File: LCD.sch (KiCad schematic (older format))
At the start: 5 parts

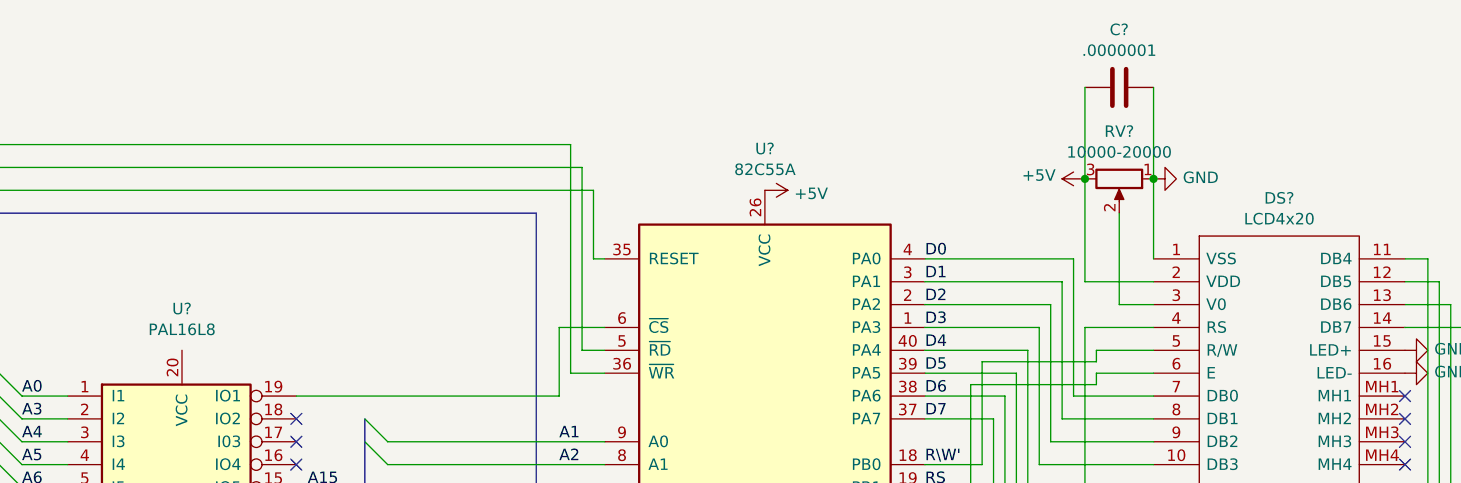
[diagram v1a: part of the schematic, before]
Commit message: All schematics present
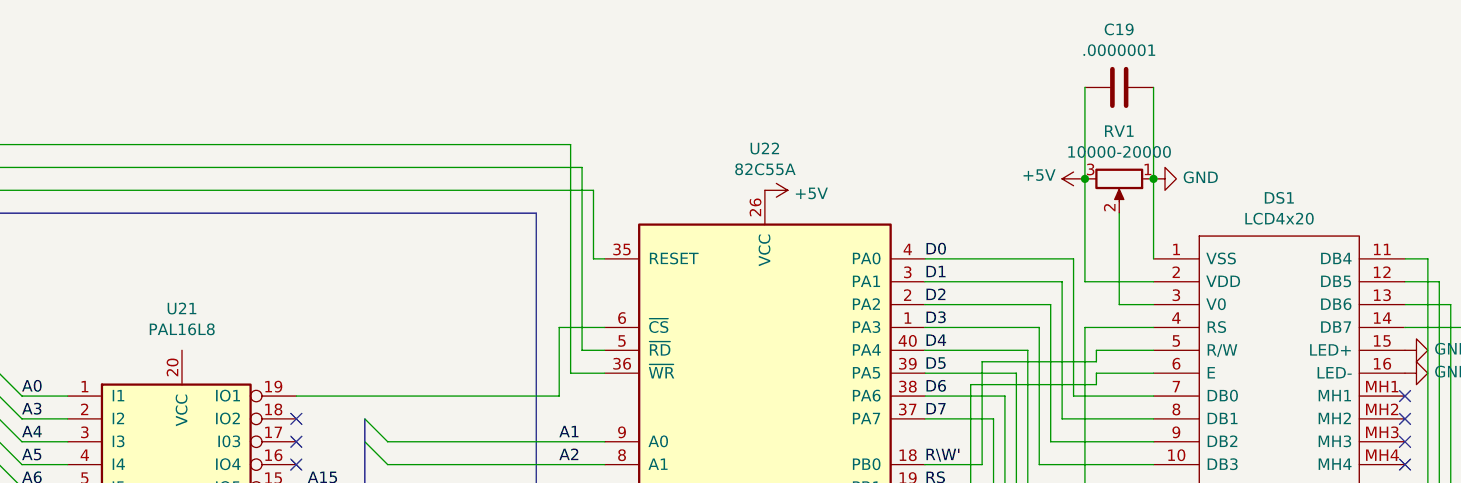
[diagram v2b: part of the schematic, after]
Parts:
- gave numbers to parts that had none: 5
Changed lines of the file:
@@
 $Descr A4 11693 8268
 encoding utf-8
-Sheet 9 9
+Sheet 9 12
 Title ""
 Date ""
@@
 $EndDescr
 $Comp
-L LCD4x20:LCD4x20 DS?
+L LCD4x20:LCD4x20 DS1
 U 1 1 61C38556
 P 7300 2900
-F 0 "DS?" H 7850 3165 50  0000 C CNN
+F 0 "DS1" H 7850 3165 50  0000 C CNN
 F 1 "LCD4x20" H 7850 3074 50  0000 C CNN
 F 2 "LCD4x20" H 8250 3000 50  0001 L CNN
@@
 $EndComp
 $Comp
-L Logic_Programmable:PAL16L8 U?
+L Logic_Programmable:PAL16L8 U21
 U 1 1 61C4A6F2
 P 3050 4000
-F 0 "U?" H 3050 4881 50  0000 C CNN
+F 0 "U21" H 3050 4881 50  0000 C CNN
 F 1 "PAL16L8" H 3050 4790 50  0000 C CNN
 F 2 "" H 3050 4000 50  0001 C CNN
@@
 	3550 3900 3750 3900
 $Comp
-L Interface:82C55A U?
+L Interface:82C55A U22
 U 1 1 61C54085
 P 5600 4200
-F 0 "U?" H 5600 5981 50  0000 C CNN
+F 0 "U22" H 5600 5981 50  0000 C CNN
 F 1 "82C55A" H 5600 5890 50  0000 C CNN
 F 2 "Package_DIP:DIP-40_W15.24mm" H 5600 4500 50  0001 C CNN
@@
 A15
 $Comp
-L power:GND #PWR?
+L power:GND #PWR0104
 U 1 1 61C82614
 P 5600 5800
-F 0 "#PWR?" H 5600 5550 50  0001 C CNN
+F 0 "#PWR0104" H 5600 5550 50  0001 C CNN
 F 1 "GND" H 5605 5627 50  0000 C CNN
 F 2 "" H 5600 5800 50  0001 C CNN
@@
 $EndComp
 $Comp
-L power:+5V #PWR?
+L power:+5V #PWR0105
 U 1 1 61C82872
 P 5600 2600
-F 0 "#PWR?" H 5600 2450 50  0001 C CNN
+F 0 "#PWR0105" H 5600 2450 50  0001 C CNN
 F 1 "+5V" V 5615 2728 50  0000 L CNN
 F 2 "" H 5600 2600 50  0001 C CNN
@@
 NoConn ~ 8400 3800
 $Comp
-L power:GND #PWR?
+L power:GND #PWR0106
 U 1 1 61C9440B
 P 8400 3300
-F 0 "#PWR?" H 8400 3050 50  0001 C CNN
+F 0 "#PWR0106" H 8400 3050 50  0001 C CNN
 F 1 "GND" V 8405 3172 50  0000 R CNN
 F 2 "" H 8400 3300 50  0001 C CNN
@@
 $EndComp
 $Comp
-L power:GND #PWR?
+L power:GND #PWR0107
 U 1 1 61C94FF9
 P 8400 3400
-F 0 "#PWR?" H 8400 3150 50  0001 C CNN
+F 0 "#PWR0107" H 8400 3150 50  0001 C CNN
 F 1 "GND" V 8405 3272 50  0000 R CNN
 F 2 "" H 8400 3400 50  0001 C CNN
@@
 	7150 3100 7150 2700
 $Comp
-L Device:R_POT RV?
+L Device:R_POT RV1
 U 1 1 61CC45A4
 P 7150 2550
-F 0 "RV?" V 6943 2550 50  0000 C CNN
+F 0 "RV1" V 6943 2550 50  0000 C CNN
 F 1 "10000-20000" V 7034 2550 50  0000 C CNN
 F 2 "" H 7150 2550 50  0001 C CNN
@@
 	7300 2550 7300 2900
 $Comp
-L power:GND #PWR?
+L power:GND #PWR0108
 U 1 1 61CCF39A
 P 7300 2550
-F 0 "#PWR?" H 7300 2300 50  0001 C CNN
+F 0 "#PWR0108" H 7300 2300 50  0001 C CNN
 F 1 "GND" V 7305 2422 50  0000 R CNN
 F 2 "" H 7300 2550 50  0001 C CNN
@@
 $EndComp
 $Comp
-L power:+5V #PWR?
+L power:+5V #PWR0109
 U 1 1 61CD158F
 P 7000 2550
-F 0 "#PWR?" H 7000 2400 50  0001 C CNN
+F 0 "#PWR0109" H 7000 2400 50  0001 C CNN
 F 1 "+5V" V 7015 2678 50  0000 L CNN
 F 2 "" H 7000 2550 50  0001 C CNN
@@
 $EndComp
 $Comp
-L Device:C C?
+L Device:C C19
 U 1 1 61CD27EB
 P 7150 2150
-F 0 "C?" V 6898 2150 50  0000 C CNN
+F 0 "C19" V 6898 2150 50  0000 C CNN
 F 1 ".0000001" V 6989 2150 50  0000 C CNN
 F 2 "" H 7188 2000 50  0001 C CNN

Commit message: Fixing Weirdness
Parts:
- added C34, C35: 0.1uF, symbol Device:C
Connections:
- net +5V: now also U21.20 (VCC), C34.1, C35.1
- net GND: now also U21.10 (GND), C34.2, C35.2
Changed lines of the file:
@@
 $Descr A4 11693 8268
 encoding utf-8
-Sheet 9 13
+Sheet 8 13
 Title ""
 Date ""
@@
 RESET
 Text HLabel 1900 2700 0    50   Input ~ 0
-Data
+D[0...15]
 Text HLabel 1900 2800 0    50   Input ~ 0
-Address
+A[0...19]
 NoConn ~ 8400 3500
 NoConn ~ 8400 3600
@@
 Wire Wire Line
 	7300 2150 7300 2550
+$Comp
+L power:GND #PWR089
+U 1 1 61B9F368
+P 3050 4600
+F 0 "#PWR089" H 3050 4350 50  0001 C CNN
+F 1 "GND" V 3055 4472 50  0000 R CNN
+F 2 "" H 3050 4600 50  0001 C CNN
+F 3 "" H 3050 4600 50  0001 C CNN
+	1    3050 4600
+	0    1    1    0
+$EndComp
+$Comp
+L power:GND #PWR083
+U 1 1 61B9F48A
+P 2550 3300
+F 0 "#PWR083" H 2550 3050 50  0001 C CNN
+F 1 "GND" V 2555 3172 50  0000 R CNN
+F 2 "" H 2550 3300 50  0001 C CNN
+F 3 "" H 2550 3300 50  0001 C CNN
+	1    2550 3300
+	0    1    1    0
+$EndComp
+$Comp
+L Device:C C34
+U 1 1 61B9F9C2
+P 2700 3300
+F 0 "C34" V 2448 3300 50  0000 C CNN
+F 1 "0.1uF" V 2539 3300 50  0000 C CNN
+F 2 "" H 2738 3150 50  0001 C CNN
+F 3 "~" H 2700 3300 50  0001 C CNN
+	1    2700 3300
+	0    1    1    0
+$EndComp
+Wire Wire Line
+	2850 3300 3050 3300
+$Comp
+L power:+5V #PWR084
+U 1 1 61BA292A
+P 3050 3300
+F 0 "#PWR084" H 3050 3150 50  0001 C CNN
+F 1 "+5V" V 3065 3428 50  0000 L CNN
+F 2 "" H 3050 3300 50  0001 C CNN
+F 3 "" H 3050 3300 50  0001 C CNN
+	1    3050 3300
+	0    1    1    0
+$EndComp
+Connection ~ 3050 3300
+$Comp
+L power:GND #PWR090
+U 1 1 61BA833A
+P 5200 2600
+F 0 "#PWR090" H 5200 2350 50  0001 C CNN
+F 1 "GND" V 5205 2472 50  0000 R CNN
+F 2 "" H 5200 2600 50  0001 C CNN
+F 3 "" H 5200 2600 50  0001 C CNN
+	1    5200 2600
+	0    1    1    0
+$EndComp
+$Comp
+L Device:C C35
+U 1 1 61BA84C6
+P 5350 2600
+F 0 "C35" V 5098 2600 50  0000 C CNN
+F 1 "0.1uF" V 5189 2600 50  0000 C CNN
+F 2 "" H 5388 2450 50  0001 C CNN
+F 3 "~" H 5350 2600 50  0001 C CNN
+	1    5350 2600
+	0    1    1    0
+$EndComp
+Wire Wire Line
+	5500 2600 5600 2600
 Wire Bus Line
 	3850 3600 3850 4750
@@
 Wire Bus Line
 	2250 2800 2250 4750
+Connection ~ 5600 2600
 $EndSCHEMATC

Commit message: Started PCB
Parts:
- C26: renamed from C34; footprint (none) -> Capacitor_SMD:CP_Elec_3x5.3
- C27: renamed from C35; footprint (none) -> Capacitor_SMD:CP_Elec_3x5.3
- C28: renamed from C19; footprint (none) -> Capacitor_SMD:CP_Elec_3x5.3
- DS1: footprint LCD4x20 -> parts:LCD4x20
- RV1: footprint (none) -> Potentiometer_SMD:Potentiometer_ACP_CA6-VSMD_Vertical
- U20: renamed from U21; footprint (none) -> Package_DIP:DIP-20_W7.62mm
- renumbered U22 to U21
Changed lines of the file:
@@
 F 0 "DS1" H 7850 3165 50  0000 C CNN
 F 1 "LCD4x20" H 7850 3074 50  0000 C CNN
-F 2 "LCD4x20" H 8250 3000 50  0001 L CNN
+F 2 "parts:LCD4x20" H 8250 3000 50  0001 L CNN
 F 3 "https://componentsearchengine.com/Datasheets/1/LCD4x20.pdf" H 8250 2900 50  0001 L CNN
 F 4 "LCD Character Display Modules & Accessories STN-Y/G Transfl 77.5 x 47.0" H 8250 2800 50  0001 L CNN "Description"
@@
 $EndComp
 $Comp
-L Logic_Programmable:PAL16L8 U21
+L Logic_Programmable:PAL16L8 U20
 U 1 1 61C4A6F2
 P 3050 4000
-F 0 "U21" H 3050 4881 50  0000 C CNN
+F 0 "U20" H 3050 4881 50  0000 C CNN
 F 1 "PAL16L8" H 3050 4790 50  0000 C CNN
-F 2 "" H 3050 4000 50  0001 C CNN
+F 2 "Package_DIP:DIP-20_W7.62mm" H 3050 4000 50  0001 C CNN
 F 3 "" H 3050 4000 50  0001 C CNN
 	1    3050 4000
@@
 	3550 3900 3750 3900
 $Comp
-L Interface:82C55A U22
+L Interface:82C55A U21
 U 1 1 61C54085
 P 5600 4200
-F 0 "U22" H 5600 5981 50  0000 C CNN
+F 0 "U21" H 5600 5981 50  0000 C CNN
 F 1 "82C55A" H 5600 5890 50  0000 C CNN
 F 2 "Package_DIP:DIP-40_W15.24mm" H 5600 4500 50  0001 C CNN
@@
 A15
 $Comp
-L power:GND #PWR0104
+L power:GND #PWR0100
 U 1 1 61C82614
 P 5600 5800
-F 0 "#PWR0104" H 5600 5550 50  0001 C CNN
+F 0 "#PWR0100" H 5600 5550 50  0001 C CNN
 F 1 "GND" H 5605 5627 50  0000 C CNN
 F 2 "" H 5600 5800 50  0001 C CNN
@@
 $EndComp
 $Comp
-L power:+5V #PWR0105
+L power:+5V #PWR099
 U 1 1 61C82872
 P 5600 2600
-F 0 "#PWR0105" H 5600 2450 50  0001 C CNN
+F 0 "#PWR099" H 5600 2450 50  0001 C CNN
 F 1 "+5V" V 5615 2728 50  0000 L CNN
 F 2 "" H 5600 2600 50  0001 C CNN
@@
 NoConn ~ 8400 3800
 $Comp
-L power:GND #PWR0106
+L power:GND #PWR0103
 U 1 1 61C9440B
 P 8400 3300
-F 0 "#PWR0106" H 8400 3050 50  0001 C CNN
+F 0 "#PWR0103" H 8400 3050 50  0001 C CNN
 F 1 "GND" V 8405 3172 50  0000 R CNN
 F 2 "" H 8400 3300 50  0001 C CNN
@@
 $EndComp
 $Comp
-L power:GND #PWR0107
+L power:GND #PWR0104
 U 1 1 61C94FF9
 P 8400 3400
-F 0 "#PWR0107" H 8400 3150 50  0001 C CNN
+F 0 "#PWR0104" H 8400 3150 50  0001 C CNN
 F 1 "GND" V 8405 3272 50  0000 R CNN
 F 2 "" H 8400 3400 50  0001 C CNN
@@
 F 0 "RV1" V 6943 2550 50  0000 C CNN
 F 1 "10000-20000" V 7034 2550 50  0000 C CNN
-F 2 "" H 7150 2550 50  0001 C CNN
+F 2 "Potentiometer_SMD:Potentiometer_ACP_CA6-VSMD_Vertical" H 7150 2550 50  0001 C CNN
 F 3 "~" H 7150 2550 50  0001 C CNN
 	1    7150 2550
@@
 	7300 2550 7300 2900
 $Comp
-L power:GND #PWR0108
+L power:GND #PWR0102
 U 1 1 61CCF39A
 P 7300 2550
-F 0 "#PWR0108" H 7300 2300 50  0001 C CNN
+F 0 "#PWR0102" H 7300 2300 50  0001 C CNN
 F 1 "GND" V 7305 2422 50  0000 R CNN
 F 2 "" H 7300 2550 50  0001 C CNN
@@
 $EndComp
 $Comp
-L power:+5V #PWR0109
+L power:+5V #PWR0101
 U 1 1 61CD158F
 P 7000 2550
-F 0 "#PWR0109" H 7000 2400 50  0001 C CNN
+F 0 "#PWR0101" H 7000 2400 50  0001 C CNN
 F 1 "+5V" V 7015 2678 50  0000 L CNN
 F 2 "" H 7000 2550 50  0001 C CNN
@@
 $EndComp
 $Comp
-L Device:C C19
+L Device:C C28
 U 1 1 61CD27EB
 P 7150 2150
-F 0 "C19" V 6898 2150 50  0000 C CNN
+F 0 "C28" V 6898 2150 50  0000 C CNN
 F 1 ".0000001" V 6989 2150 50  0000 C CNN
-F 2 "" H 7188 2000 50  0001 C CNN
+F 2 "Capacitor_SMD:CP_Elec_3x5.3" H 7188 2000 50  0001 C CNN
 F 3 "~" H 7150 2150 50  0001 C CNN
 	1    7150 2150
@@
 	7300 2150 7300 2550
 $Comp
-L power:GND #PWR089
+L power:GND #PWR097
 U 1 1 61B9F368
 P 3050 4600
-F 0 "#PWR089" H 3050 4350 50  0001 C CNN
+F 0 "#PWR097" H 3050 4350 50  0001 C CNN
 F 1 "GND" V 3055 4472 50  0000 R CNN
 F 2 "" H 3050 4600 50  0001 C CNN
@@
 $EndComp
 $Comp
-L power:GND #PWR083
+L power:GND #PWR095
 U 1 1 61B9F48A
 P 2550 3300
-F 0 "#PWR083" H 2550 3050 50  0001 C CNN
+F 0 "#PWR095" H 2550 3050 50  0001 C CNN
 F 1 "GND" V 2555 3172 50  0000 R CNN
 F 2 "" H 2550 3300 50  0001 C CNN
@@
 $EndComp
 $Comp
-L Device:C C34
+L Device:C C26
 U 1 1 61B9F9C2
 P 2700 3300
-F 0 "C34" V 2448 3300 50  0000 C CNN
+F 0 "C26" V 2448 3300 50  0000 C CNN
 F 1 "0.1uF" V 2539 3300 50  0000 C CNN
-F 2 "" H 2738 3150 50  0001 C CNN
+F 2 "Capacitor_SMD:CP_Elec_3x5.3" H 2738 3150 50  0001 C CNN
 F 3 "~" H 2700 3300 50  0001 C CNN
 	1    2700 3300
@@
 	2850 3300 3050 3300
 $Comp
-L power:+5V #PWR084
+L power:+5V #PWR096
 U 1 1 61BA292A
 P 3050 3300
-F 0 "#PWR084" H 3050 3150 50  0001 C CNN
+F 0 "#PWR096" H 3050 3150 50  0001 C CNN
 F 1 "+5V" V 3065 3428 50  0000 L CNN
 F 2 "" H 3050 3300 50  0001 C CNN
@@
 Connection ~ 3050 3300
 $Comp
-L power:GND #PWR090
+L power:GND #PWR098
 U 1 1 61BA833A
 P 5200 2600
-F 0 "#PWR090" H 5200 2350 50  0001 C CNN
+F 0 "#PWR098" H 5200 2350 50  0001 C CNN
 F 1 "GND" V 5205 2472 50  0000 R CNN
 F 2 "" H 5200 2600 50  0001 C CNN
@@
 $EndComp
 $Comp
-L Device:C C35
+L Device:C C27
 U 1 1 61BA84C6
 P 5350 2600
-F 0 "C35" V 5098 2600 50  0000 C CNN
+F 0 "C27" V 5098 2600 50  0000 C CNN
 F 1 "0.1uF" V 5189 2600 50  0000 C CNN
-F 2 "" H 5388 2450 50  0001 C CNN
+F 2 "Capacitor_SMD:CP_Elec_3x5.3" H 5388 2450 50  0001 C CNN
 F 3 "~" H 5350 2600 50  0001 C CNN
 	1    5350 2600
@@
 Wire Wire Line
 	5500 2600 5600 2600
+Connection ~ 5600 2600
 Wire Bus Line
 	3850 3600 3850 4750
@@
 Wire Bus Line
 	2250 2800 2250 4750
-Connection ~ 5600 2600
 $EndSCHEMATC

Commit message: Readd LCD changes.
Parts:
- removed C26, C27: 0.1uF, Capacitor_SMD:CP_Elec_3x5.3, symbol Device:C
- removed U20: PAL16L8, Package_DIP:DIP-20_W7.62mm, symbol Logic_Programmable:PAL16L8
- removed U21: 82C55A, Package_DIP:DIP-40_W15.24mm, symbol Interface:82C55A
- added C?: 0.1uF, symbol Device:C
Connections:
- net +5V: now also C?.2
- net D0 renamed D[0]
- net D1 renamed D[1]
- net D2 renamed D[2]
- net D3 renamed D[3]
- net D4 renamed D[4]
- net D5 renamed D[5]
- net D6 renamed D[6]
- net D7 renamed D[7]
- net E: no longer names the net of DS1.6 (E)
- net E: now also C?.1
- net RS renamed A[1]
- net R\W' renamed A[2]
- no-connect marks 20 -> 4

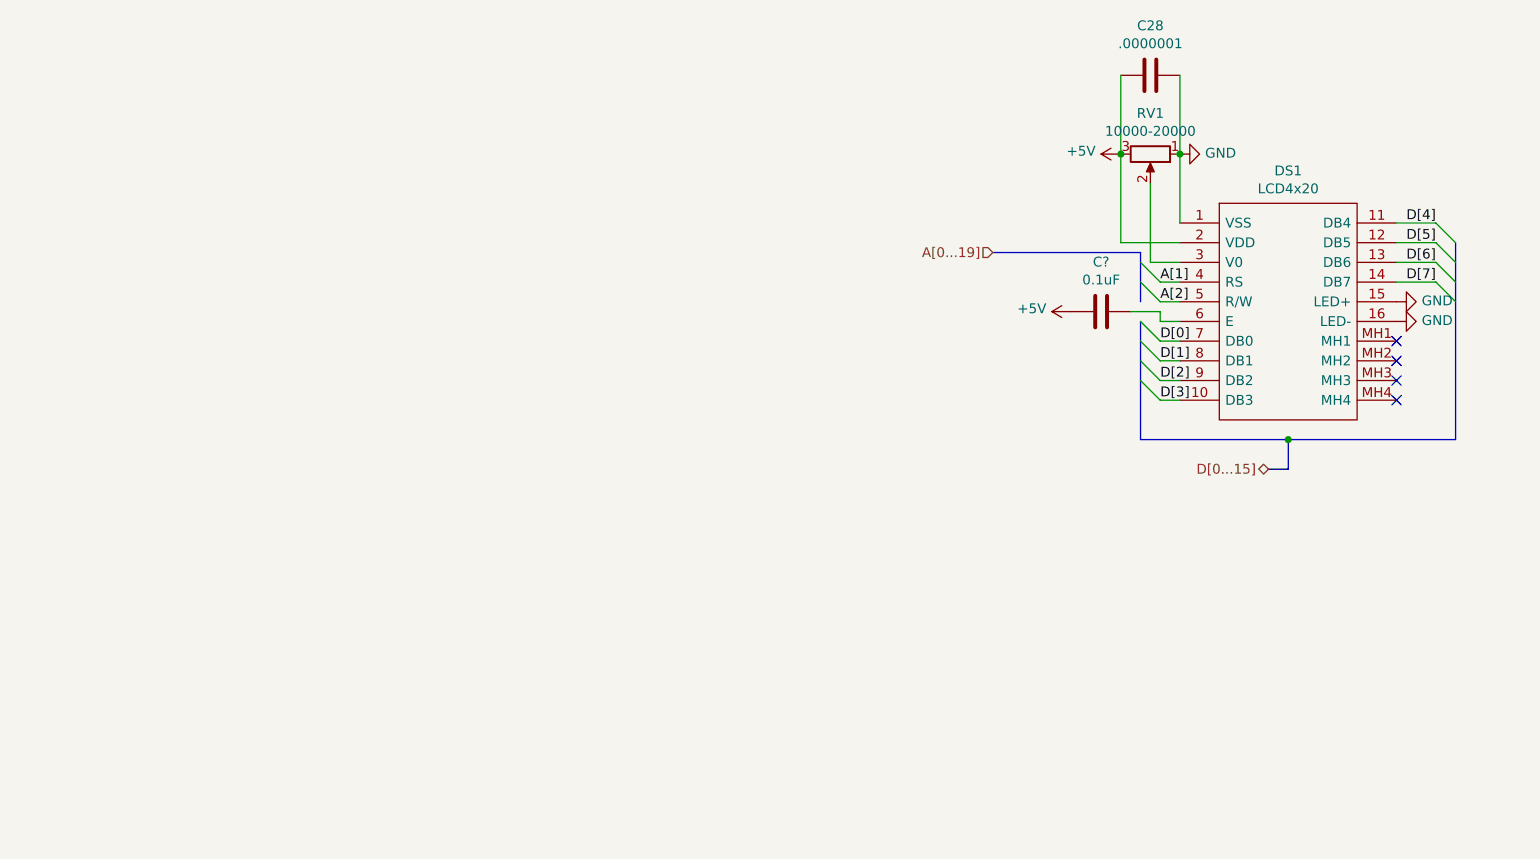
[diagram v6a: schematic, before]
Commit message: LCD fixed
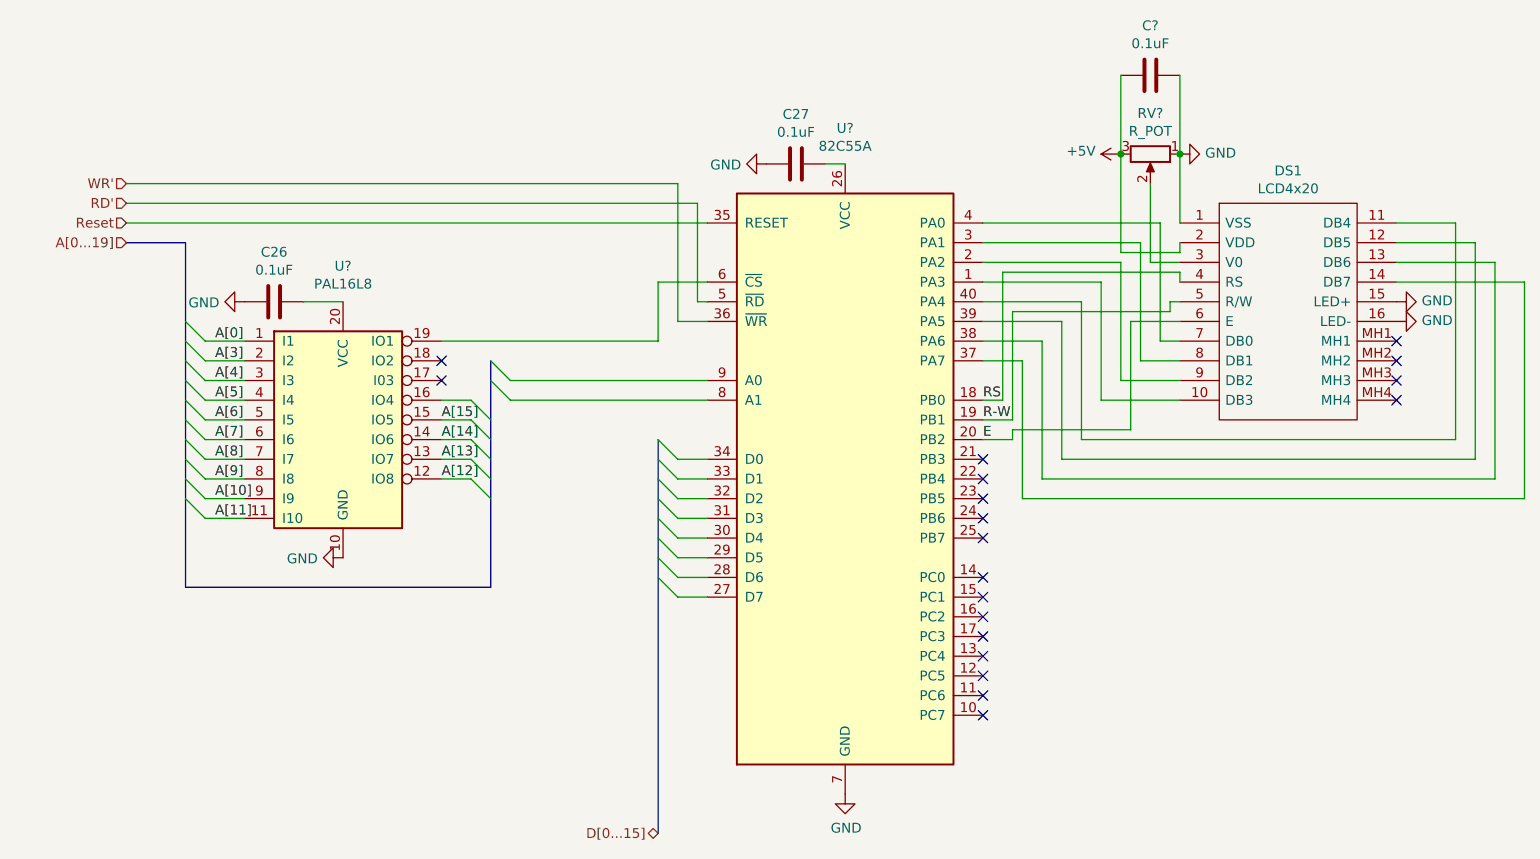
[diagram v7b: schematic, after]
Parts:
- removed C28: .0000001, Capacitor_SMD:CP_Elec_3x5.3, symbol Device:C
- removed C?: 0.1uF, symbol Device:C
- removed RV1: 10000-20000, Potentiometer_SMD:Potentiometer_ACP_CA6-VSMD_Vertical, symbol Device:R_POT
- added C26, C27: 0.1uF, Capacitor_SMD:CP_Elec_3x5.3, symbol Device:C
- added C?: 0.1uF, symbol Device:C
- added RV?: R_POT, symbol Device:R_POT
- added U?: PAL16L8, symbol Logic_Programmable:PAL16L8
- added U?: 82C55A, Package_DIP:DIP-40_W15.24mm, symbol Interface:82C55A
- DS1: Manufacturer_Name Newhaven Display -> (none); Mouser Part Number 763-0420AZFLYBW33V3 -> (none); Mouser Price/Stock https://www.mouser.com/Search/Refine.aspx?Keyword=763-0420A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 -> (none)
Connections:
- net +5V: now also C?.2, RV?.3
- net GND: now also C26.2, C27.2, C?.1, RV?.1, U?.10 (GND), U?.7 (GND)
- net E: now reaches DS1.6 (E)
- net E: now also U?.20 (PB2)
- net at DS1.3 (V0): now also RV?.2
- net A[1] renamed RS
- net RS: now also U?.18 (PB0)
- net A[2] renamed R-W
- net R-W: now also U?.19 (PB1)
- net D[0]: no longer names the net of DS1.7 (DB0)
- net D[0]: now also U?.4 (PA0)
- net D[1]: no longer names the net of DS1.8 (DB1)
- net D[1]: now also U?.3 (PA1)
- net D[2]: no longer names the net of DS1.9 (DB2)
- net D[2]: now also U?.2 (PA2)
- net D[3]: no longer names the net of DS1.10 (DB3)
- net D[3]: now also U?.1 (PA3)
- net D[4]: no longer names the net of DS1.11 (DB4)
- net D[4]: now also U?.40 (PA4)
- net D[5]: no longer names the net of DS1.12 (DB5)
- net D[5]: now also U?.39 (PA5)
- net D[6]: no longer names the net of DS1.13 (DB6)
- net D[6]: now also U?.38 (PA6)
- net D[7]: no longer names the net of DS1.14 (DB7)
- net D[7]: now also U?.37 (PA7)
- new net: C26.1, U?.20 (VCC)
- new net: C27.1, U?.26 (VCC)
- new net: U?.19 (IO1), U?.6 (~CS~)
- new net A[0]: U?.1 (I1)
- new net A[10]: U?.9 (I9)
- new net A[11]: U?.11 (I10)
- new net A[12]: U?.12 (IO8)
- new net A[13]: U?.13 (IO7)
- new net A[14]: U?.14 (IO6)
- new net A[15]: U?.15 (IO5)
- new net A[3]: U?.2 (I2)
- new net A[4]: U?.3 (I3)
- new net A[5]: U?.4 (I4)
- new net A[6]: U?.5 (I5)
- new net A[7]: U?.6 (I6)
- new net A[8]: U?.7 (I7)
- new net A[9]: U?.8 (I8)
- new net RD': U?.5 (~RD~)
- new net Reset: U?.35 (RESET)
- new net WR': U?.36 (~WR~)
- no-connect marks 4 -> 19
